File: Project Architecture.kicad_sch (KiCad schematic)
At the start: 0 parts

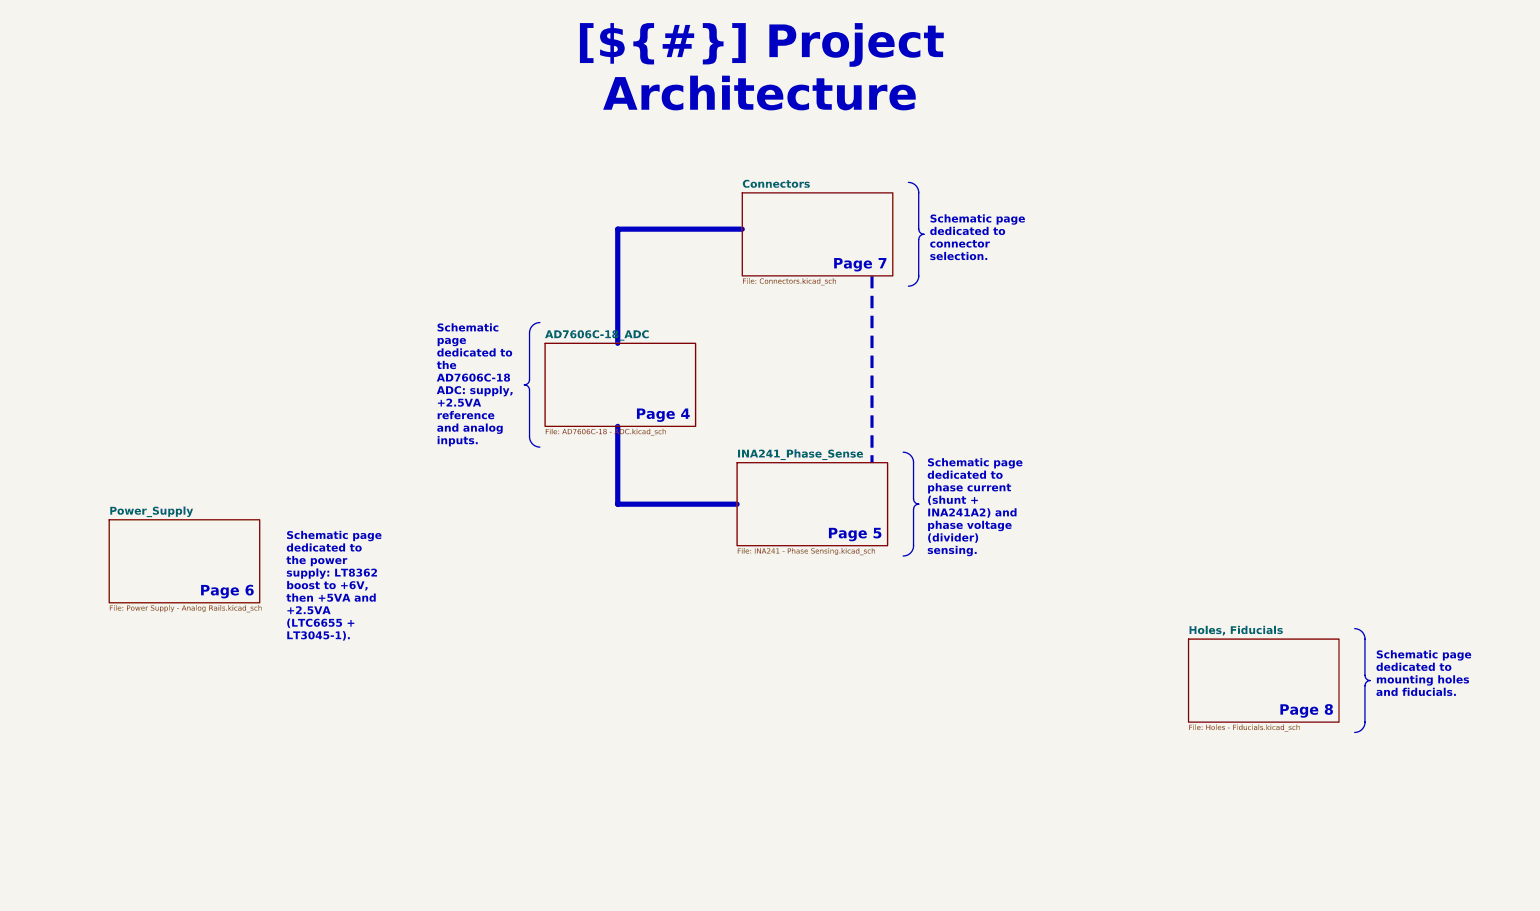
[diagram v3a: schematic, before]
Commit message: Fix the +2.5VA reference, add XT60PW-M connectors, predict measurement quality
- IC3: LTC6655LN-2.5 replaced by the standard LTC6655-2.5, pin 6 is now
  VOUT_S tied to VOUT_F (the LN version has NR on that pin)
- R12: 49.9k -> 24.9k on the SET pin of IC9, +2.5VA = 2.500 V instead of
  2.549 V; both points removed from the README design review
- J5, J6: two Amass XT60PW-M added on the Connectors sheet and on the PCB,
  with symbol, footprint and 3D model in lib/. Their power pins are not
  wired yet
- Simulations 07 (ESC PWM waveforms through both channels) and 08 (Monte
  Carlo on the tolerances), analysed by measurement_quality.py into
  measurement_quality.md; plot style shared in plotstyle.py
- Simulations 01, 02, 04, results.md and their figures redone for the
  corrected rail
- README, README template and CHANGELOG updated; all sheets re-saved from
  KiCad

Co-Authored-By: Claude Opus 5.5 <noreply@anthropic.com>
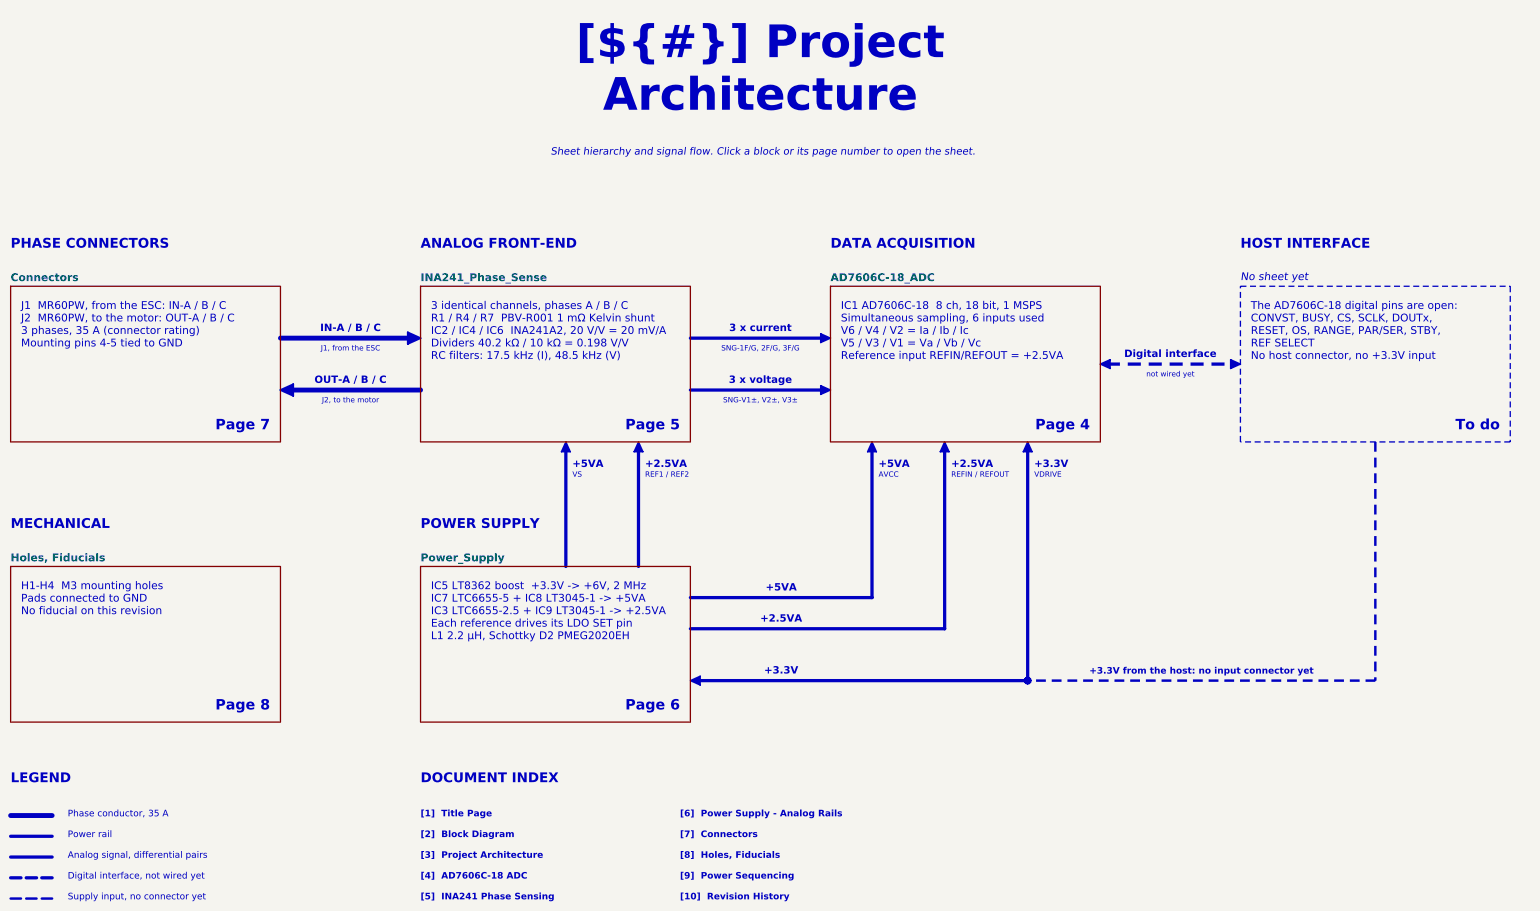
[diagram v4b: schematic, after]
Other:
- note added: "+2.5VA"
- note added: "+3.3V"
- note added: "+3.3V from the host: no input connector yet"
- note added: "+5VA"
- note added: "3 identical channels, phases A / B / C R1 / R4 / R7 PBV-R001 1 mΩ Kelvin shunt IC2 / IC4 / IC6 INA241A2, 20 V/V = 20 mV/A Dividers 40.2 kΩ / 10 kΩ = 0.198 V/V RC filters: 17.5 kHz (I), 48.5 kHz (V)"
- note added: "3 x current"
- note added: "3 x voltage"
- note added: "ANALOG FRONT-END"
- note added: "AVCC"
- note added: "Analog signal, differential pairs"
- note added: "DATA ACQUISITION"
- note added: "DOCUMENT INDEX"
- note added: "Digital interface"
- note added: "Digital interface, not wired yet"
- note added: "H1-H4 M3 mounting holes Pads connected to GND No fiducial on this revision"
- note added: "HOST INTERFACE"
- note added: "IC1 AD7606C-18 8 ch, 18 bit, 1 MSPS Simultaneous sampling, 6 inputs used V6 / V4 / V2 = Ia / Ib / Ic V5 / V3 / V1 = Va / Vb / Vc Reference input REFIN/REFOUT = +2.5VA"
- note added: "IC5 LT8362 boost +3.3V -> +6V, 2 MHz IC7 LTC6655-5 + IC8 LT3045-1 -> +5VA IC3 LTC6655-2.5 + IC9 LT3045-1 -> +2.5VA Each reference drives its LDO SET pin L1 2.2 µH, Schottky D2 PMEG2020EH"
- note added: "IN-A / B / C"
- note added: "J1 MR60PW, from the ESC: IN-A / B / C J2 MR60PW, to the motor: OUT-A / B / C 3 phases, 35 A (connector rating) Mounting pins 4-5 tied to GND"
- note added: "J1, from the ESC"
- note added: "J2, to the motor"
- note added: "LEGEND"
- note added: "MECHANICAL"
- note added: "No sheet yet"
- note added: "OUT-A / B / C"
- note added: "PHASE CONNECTORS"
- note added: "POWER SUPPLY"
- note added: "Phase conductor, 35 A"
- note added: "Power rail"
- note added: "REF1 / REF2"
- note added: "REFIN / REFOUT"
- note added: "SNG-1F/G, 2F/G, 3F/G"
- note added: "SNG-V1±, V2±, V3±"
- note added: "Sheet hierarchy and signal flow. Click a block or its page number to open the sheet."
- note added: "Supply input, no connector yet"
- note added: "The AD7606C-18 digital pins are open: CONVST, BUSY, CS, SCLK, DOUTx, RESET, OS, RANGE, PAR/SER, STBY, REF SELECT No host connector, no +3.3V input"
- note added: "To do"
- note added: "VDRIVE"
- note added: "VS"
- note added: "[10] Revision History"
- note added: "[1] Title Page"
- note added: "[2] Block Diagram"
- note added: "[3] Project Architecture"
- note added: "[4] AD7606C-18 ADC"
- note added: "[5] INA241 Phase Sensing"
- note added: "[6] Power Supply - Analog Rails"
- note added: "[7] Connectors"
- note added: "[8] Holes, Fiducials"
- note added: "[9] Power Sequencing"
- note added: "not wired yet"

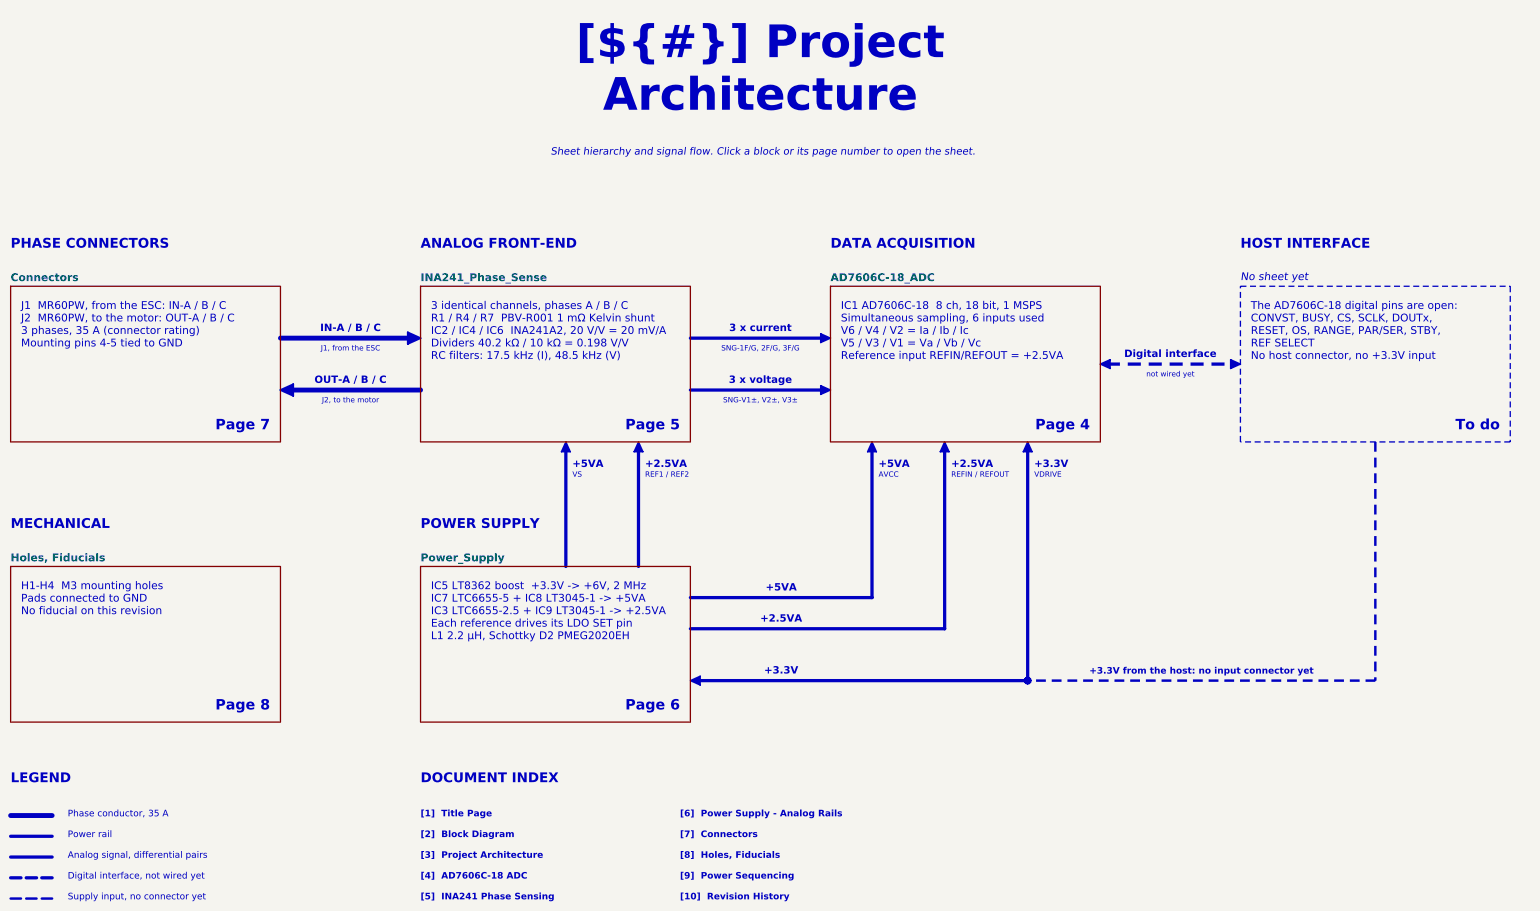
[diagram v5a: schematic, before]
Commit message: Smaller boost inductor, white board, openEMS and thermal simulations
- L1: Wurth 744373965022 (13.5 x 12.5 mm) -> WE-MAPI 4030 74438357022
  (2.2 uH, 4.1 x 4.1 x 3.1 mm, Isat 4.6 A at -10 %, above the 3.1 A LT8362
  switch limit). Footprint and STEP from the KiCad library, copied to lib/.
- Board: solder mask white (custom opaque #F4F4F0F5, the KiCad "White"
  preset renders pink over copper), silkscreen black. kibot_globals.yaml
  names the colours so the fabrication notes print WHITE / BLACK.
- Simulation/openEMS: inductance of the PBV shunts seen by the INA241
  inputs on the routed copper (results.md, figures in Images/Simulation).
- Simulation/Thermal: current density and temperature of the power paths.
- LTspice simulations, figures and README updated; sim07 DC bus figure.
- 3D animation (Images/OPEN_PHASE.mp4, OPEN_PHASE-spin.gif) on the white board.
- XT60PW-F footprint and model, bottom silkscreen cartouches.

Co-Authored-By: Claude Opus 5.5 <noreply@anthropic.com>
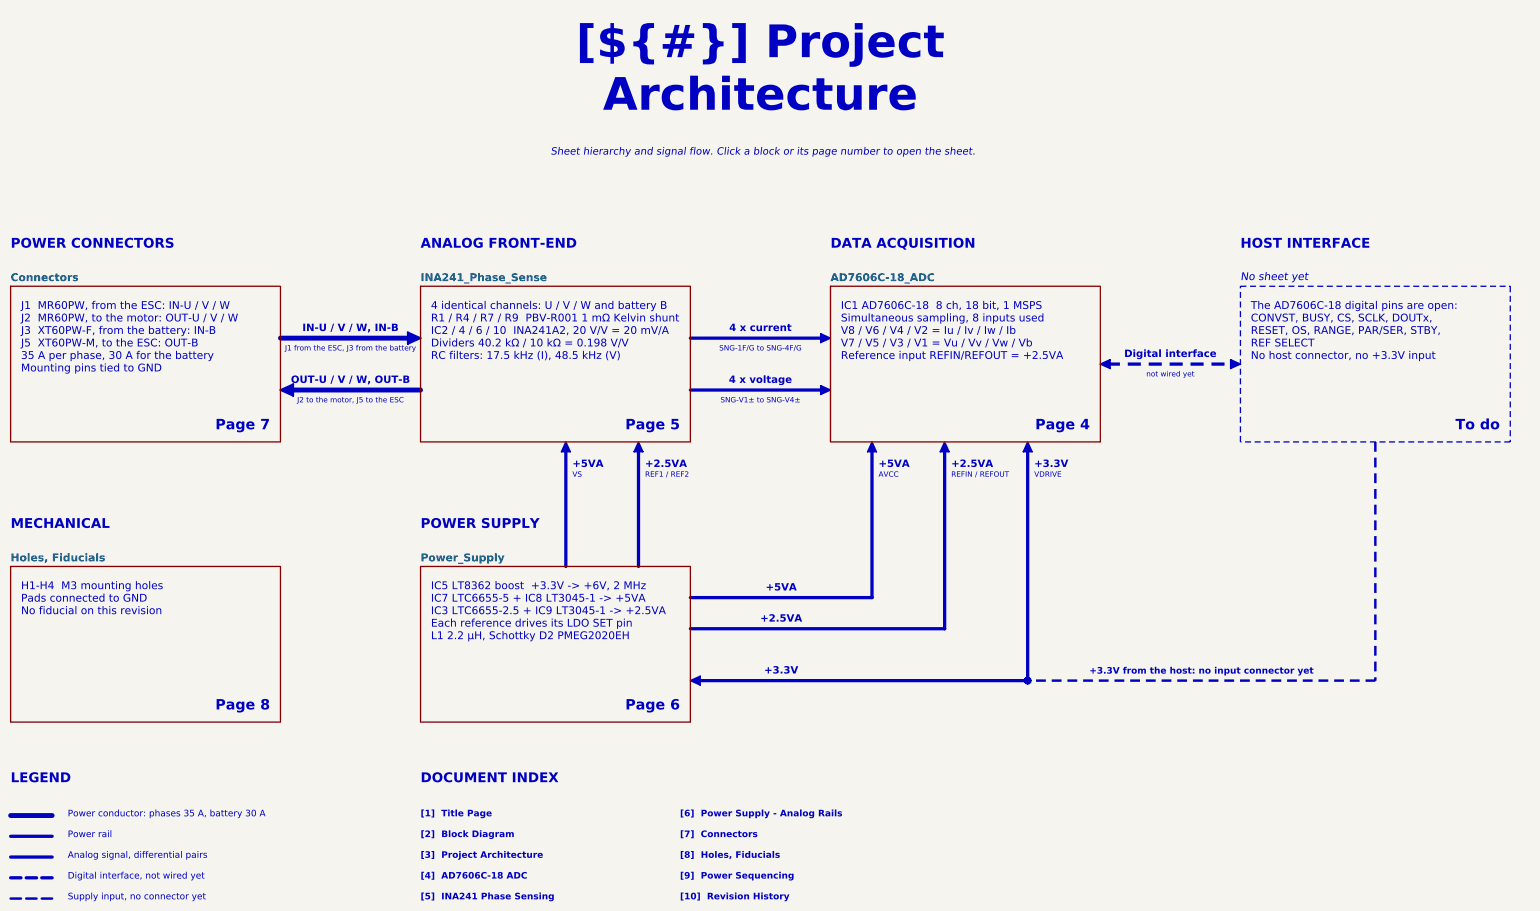
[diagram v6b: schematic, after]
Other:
- note added: "4 identical channels: U / V / W and battery B R1 / R4 / R7 / R9 PBV-R001 1 mΩ Kelvin shunt IC2 / 4 / 6 / 10 INA241A2, 20 V/V = 20 mV/A Dividers 40.2 kΩ / 10 kΩ = 0.198 V/V RC filters: 17.5 kHz (I), 48.5 kHz (V)"
- note added: "4 x current"
- note added: "4 x voltage"
- note added: "IC1 AD7606C-18 8 ch, 18 bit, 1 MSPS Simultaneous sampling, 8 inputs used V8 / V6 / V4 / V2 = Iu / Iv / Iw / Ib V7 / V5 / V3 / V1 = Vu / Vv / Vw / Vb Reference input REFIN/REFOUT = +2.5VA"
- note added: "IN-U / V / W, IN-B"
- note added: "J1 MR60PW, from the ESC: IN-U / V / W J2 MR60PW, to the motor: OUT-U / V / W J3 XT60PW-F, from the battery: IN-B J5 XT60PW-M, to the ESC: OUT-B 35 A per phase, 30 A for the battery Mounting pins tied to GND"
- note added: "J1 from the ESC, J3 from the battery"
- note added: "J2 to the motor, J5 to the ESC"
- note added: "OUT-U / V / W, OUT-B"
- note added: "POWER CONNECTORS"
- note added: "Power conductor: phases 35 A, battery 30 A"
- note added: "SNG-1F/G to SNG-4F/G"
- note added: "SNG-V1± to SNG-V4±"
- note removed: "3 identical channels, phases A / B / C R1 / R4 / R7 PBV-R001 1 mΩ Kelvin shunt IC2 / IC4 / IC6 INA241A2, 20 V/V = 20 mV/A Dividers 40.2 kΩ / 10 kΩ = 0.198 V/V RC filters: 17.5 kHz (I), 48.5 kHz (V)"
- note removed: "3 x current"
- note removed: "3 x voltage"
- note removed: "IC1 AD7606C-18 8 ch, 18 bit, 1 MSPS Simultaneous sampling, 6 inputs used V6 / V4 / V2 = Ia / Ib / Ic V5 / V3 / V1 = Va / Vb / Vc Reference input REFIN/REFOUT = +2.5VA"
- note removed: "IN-A / B / C"
- note removed: "J1 MR60PW, from the ESC: IN-A / B / C J2 MR60PW, to the motor: OUT-A / B / C 3 phases, 35 A (connector rating) Mounting pins 4-5 tied to GND"
- note removed: "J1, from the ESC"
- note removed: "J2, to the motor"
- note removed: "OUT-A / B / C"
- note removed: "PHASE CONNECTORS"
- note removed: "Phase conductor, 35 A"
- note removed: "SNG-1F/G, 2F/G, 3F/G"
- note removed: "SNG-V1±, V2±, V3±"
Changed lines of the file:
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@@
 	(title_block
 		(title "Project Architecture")
-		(date "2026-10-06")
+		(date "2026-10-11")
 		(rev "${REVISION}")
 		(company "${COMPANY}")
@@
 		)
 	)
-	(text "3 x current"
+	(text "4 x current"
 		(exclude_from_sim no)
 		(at 210.185 92.71 0)
@@
 		)
 	)
-	(text "SNG-V1±, V2±, V3±"
+	(text "SNG-V1± to SNG-V4±"
 		(exclude_from_sim no)
 		(at 210.185 108.58 0)
@@
 		)
 	)
-	(text "SNG-1F/G, 2F/G, 3F/G"
+	(text "SNG-1F/G to SNG-4F/G"
 		(exclude_from_sim no)
 		(at 210.185 95.88 0)
@@
 		)
 	)
-	(text "J1, from the ESC"
+	(text "J1 from the ESC, J3 from the battery"
 		(exclude_from_sim no)
 		(at 109.855 95.88 0)
@@
 		)
 	)
-	(text "Phase conductor, 35 A"
+	(text "Power conductor: phases 35 A, battery 30 A"
 		(exclude_from_sim no)
 		(at 40.64 211.455 0)
@@
 		)
 	)
-	(text "IC1 AD7606C-18  8 ch, 18 bit, 1 MSPS\nSimultaneous sampling, 6 inputs used\nV6 / V4 / V2 = Ia / Ib / Ic\nV5 / V3 / V1 = Va / Vb / Vc\nReference input REFIN/REFOUT = +2.5VA"
+	(text "IC1 AD7606C-18  8 ch, 18 bit, 1 MSPS\nSimultaneous sampling, 8 inputs used\nV8 / V6 / V4 / V2 = Iu / Iv / Iw / Ib\nV7 / V5 / V3 / V1 = Vu / Vv / Vw / Vb\nReference input REFIN/REFOUT = +2.5VA"
 		(exclude_from_sim no)
 		(at 229.87 85.09 0)
@@
 		)
 	)
-	(text "J2, to the motor"
+	(text "J2 to the motor, J5 to the ESC"
 		(exclude_from_sim no)
 		(at 109.855 108.58 0)
@@
 		)
 	)
-	(text "3 x voltage"
+	(text "4 x voltage"
 		(exclude_from_sim no)
 		(at 210.185 105.41 0)
@@
 		)
 	)
-	(text "IN-A / B / C"
+	(text "IN-U / V / W, IN-B"
 		(exclude_from_sim no)
 		(at 109.855 92.71 0)
@@
 		)
 	)
-	(text "PHASE CONNECTORS"
+	(text "POWER CONNECTORS"
 		(exclude_from_sim no)
 		(at 26.67 72.39 0)
@@
 		)
 	)
-	(text "J1  MR60PW, from the ESC: IN-A / B / C\nJ2  MR60PW, to the motor: OUT-A / B / C\n3 phases, 35 A (connector rating)\nMounting pins 4-5 tied to GND"
+	(text "J1  MR60PW, from the ESC: IN-U / V / W\nJ2  MR60PW, to the motor: OUT-U / V / W\nJ3  XT60PW-F, from the battery: IN-B\nJ5  XT60PW-M, to the ESC: OUT-B\n35 A per phase, 30 A for the battery\nMounting pins tied to GND"
 		(exclude_from_sim no)
 		(at 29.21 85.09 0)
@@
 		)
 	)
-	(text "OUT-A / B / C"
+	(text "OUT-U / V / W, OUT-B"
 		(exclude_from_sim no)
 		(at 109.855 105.41 0)
@@
 		)
 	)
-	(text "3 identical channels, phases A / B / C\nR1 / R4 / R7  PBV-R001 1 mΩ Kelvin shunt\nIC2 / IC4 / IC6  INA241A2, 20 V/V = 20 mV/A\nDividers 40.2 kΩ / 10 kΩ = 0.198 V/V\nRC filters: 17.5 kHz (I), 48.5 kHz (V)"
+	(text "4 identical channels: U / V / W and battery B\nR1 / R4 / R7 / R9  PBV-R001 1 mΩ Kelvin shunt\nIC2 / 4 / 6 / 10  INA241A2, 20 V/V = 20 mV/A\nDividers 40.2 kΩ / 10 kΩ = 0.198 V/V\nRC filters: 17.5 kHz (I), 48.5 kHz (V)"
 		(exclude_from_sim no)
 		(at 129.54 85.09 0)
